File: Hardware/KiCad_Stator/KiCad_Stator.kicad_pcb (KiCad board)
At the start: 4 copper layers, 28 x 28 mm, 7 parts

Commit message: feat:intro six layer
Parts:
- added H2: MountingHole, MountingHole:MountingHole_2.2mm_M2, F.Cu at (117.9, 49.3)
- added H3: MountingHole, MountingHole:MountingHole_2.2mm_M2, F.Cu at (103.8, 49.7)
- added H4: MountingHole, MountingHole:MountingHole_2.2mm_M2, F.Cu at (110.6, 57.5)
- added H5: MountingHole, MountingHole:MountingHole_2.2mm_M2, F.Cu at (102.7, 58.1)
- added H6: MountingHole, MountingHole:MountingHole_2.2mm_M2, F.Cu at (118.0, 58.3)
- A1: value B -> A
- B1: value A -> B
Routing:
- net GND: vias 9 -> 0
- net /C: vias 14 -> 29
- net /B: vias 9 -> 23
- net /A: vias 11 -> 26
- removed copper zone on B.Cu, net GND
- removed copper zone on F.Cu, net GND
- removed copper zone on In1.Cu, net GND
- removed copper zone on In2.Cu, net GND
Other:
- board size 28 x 28 mm -> 125.6 x 34.6 mm
- copper layers 4 -> 6

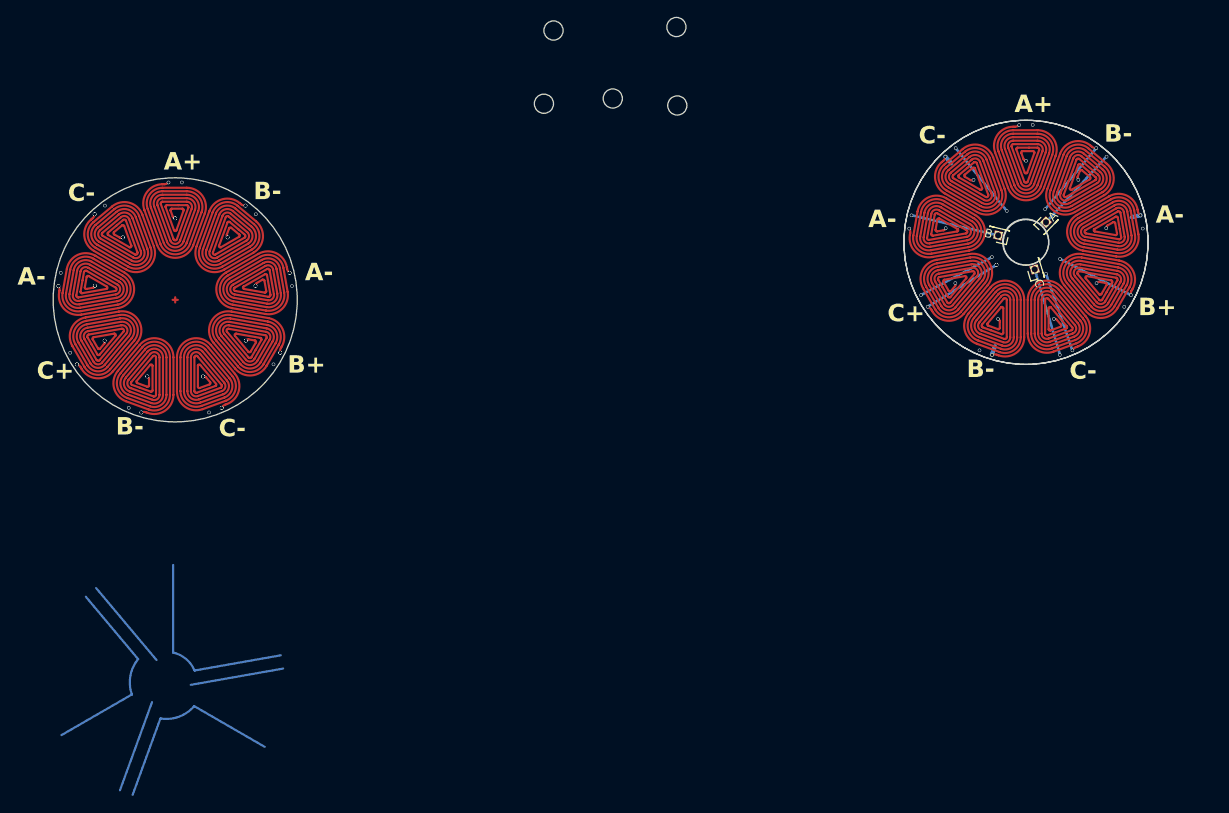
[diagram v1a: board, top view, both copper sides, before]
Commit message: stator prototype 1 finished
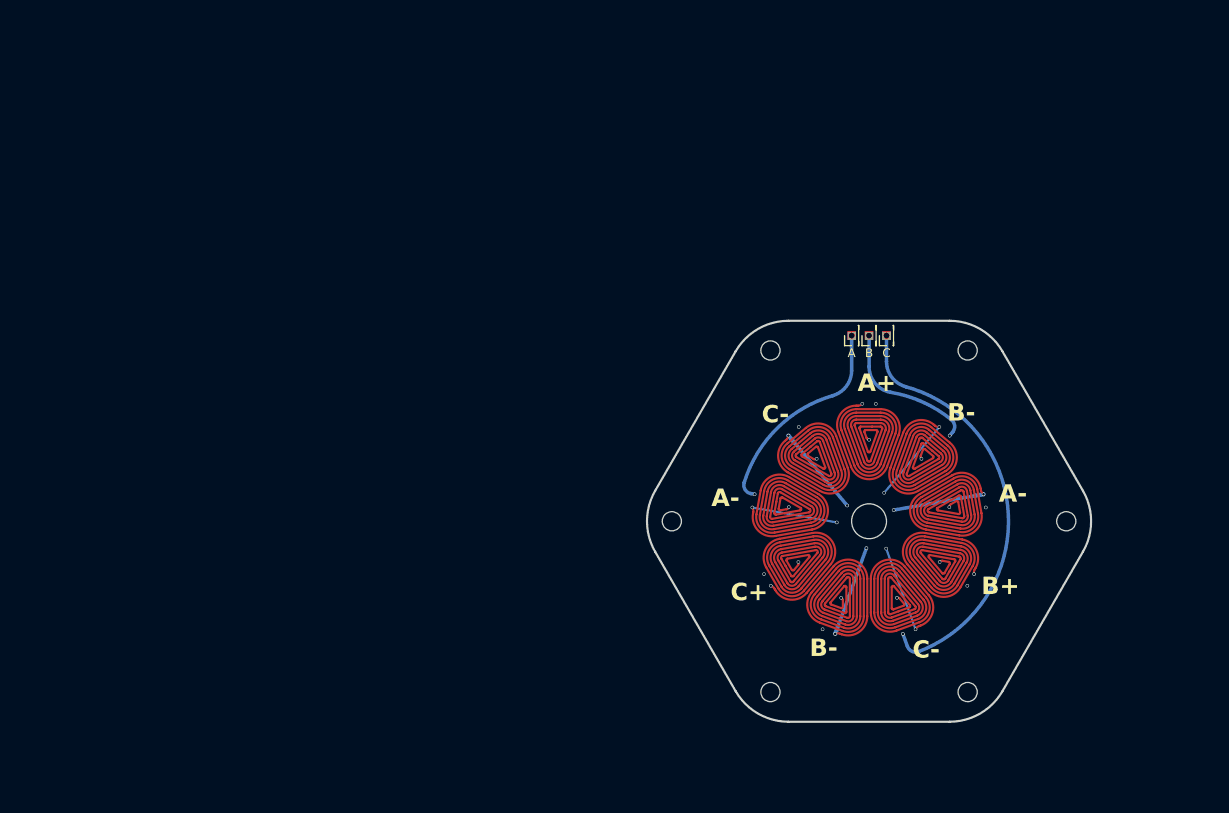
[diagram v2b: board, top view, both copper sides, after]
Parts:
- added H7: MountingHole, MountingHole:MountingHole_2.2mm_M2, F.Cu at (128.7, 125.6)
- H1: footprint MountingHole:MountingHole_5.3mm_M5 -> MountingHole:MountingHole_4mm
- moved H5 83.2 mm to (151.3, 125.6)
- moved H3 81.4 mm to (162.6, 106.0)
- moved NT2 58.6 mm to (136.3, 118.4), turned to -110 degrees
- moved H2 49.9 mm to (151.3, 86.4)
- moved H6 47.7 mm to (117.4, 106.0)
- moved NT3 36.7 mm to (131.1, 96.6), turned to 130 degrees
- moved H1 36.7 mm to (140.0, 106.0)
- moved H4 34.1 mm to (128.7, 86.4)
- moved A1 25.8 mm to (138.0, 84.7), turned to 90 degrees
- moved B1 18.7 mm to (140.0, 84.7), turned to 90 degrees
- moved C1 18.6 mm to (142.0, 84.7), turned to 90 degrees
- moved NT1 16.6 mm to (152.6, 103.0), turned to 10 degrees
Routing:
- net /B: track 4.69 -> 0.00 mm, vias 23 -> 10
- net /A: track 2.77 -> 0.00 mm, vias 26 -> 10
- net GND: vias 0 -> 3
- net /C: vias 29 -> 10
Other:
- board size 125.6 x 34.6 mm -> 51 x 46 mm
